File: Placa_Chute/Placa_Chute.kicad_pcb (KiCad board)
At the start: 2 copper layers, 87.5 x 55.5 mm, 34 parts, among them J1 Screw_Terminal_01x02, J2 Conn_01x02_Socket, J3 Conn_01x02, K1 JQC-3FF-012-1Z, Q1 IRF630, Q2 BC337, Q3 BC547, Q4 BC337, Q5 BC337, Q6 BC327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

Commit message: Apagar o esquemático de Ativação de Chute
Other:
- board outline removed
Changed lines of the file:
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@@
 		)
-	)
-	(gr_rect
-		(start 104.93 70.89)
-		(end 192.48 126.38)
-		(stroke
-			(width 0.05)
-			(type default)
-		)
-		(fill no)
-		(layer "Edge.Cuts")
 	)
 	(embedded_fonts no)

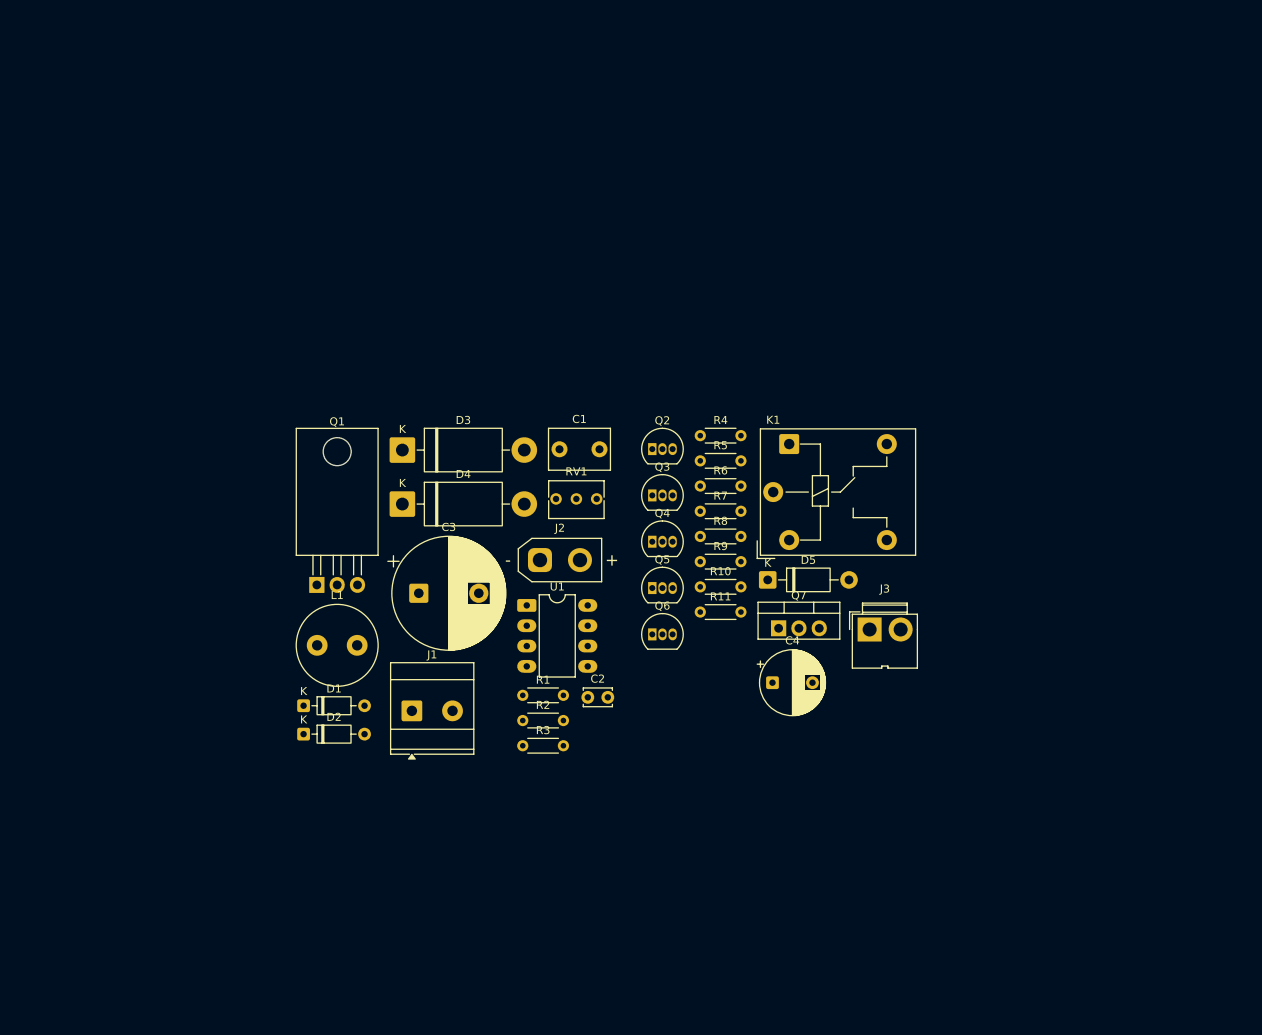
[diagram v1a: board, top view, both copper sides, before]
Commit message: Finalizando o esquemático e rearranjando a posição dos componentes na PCB
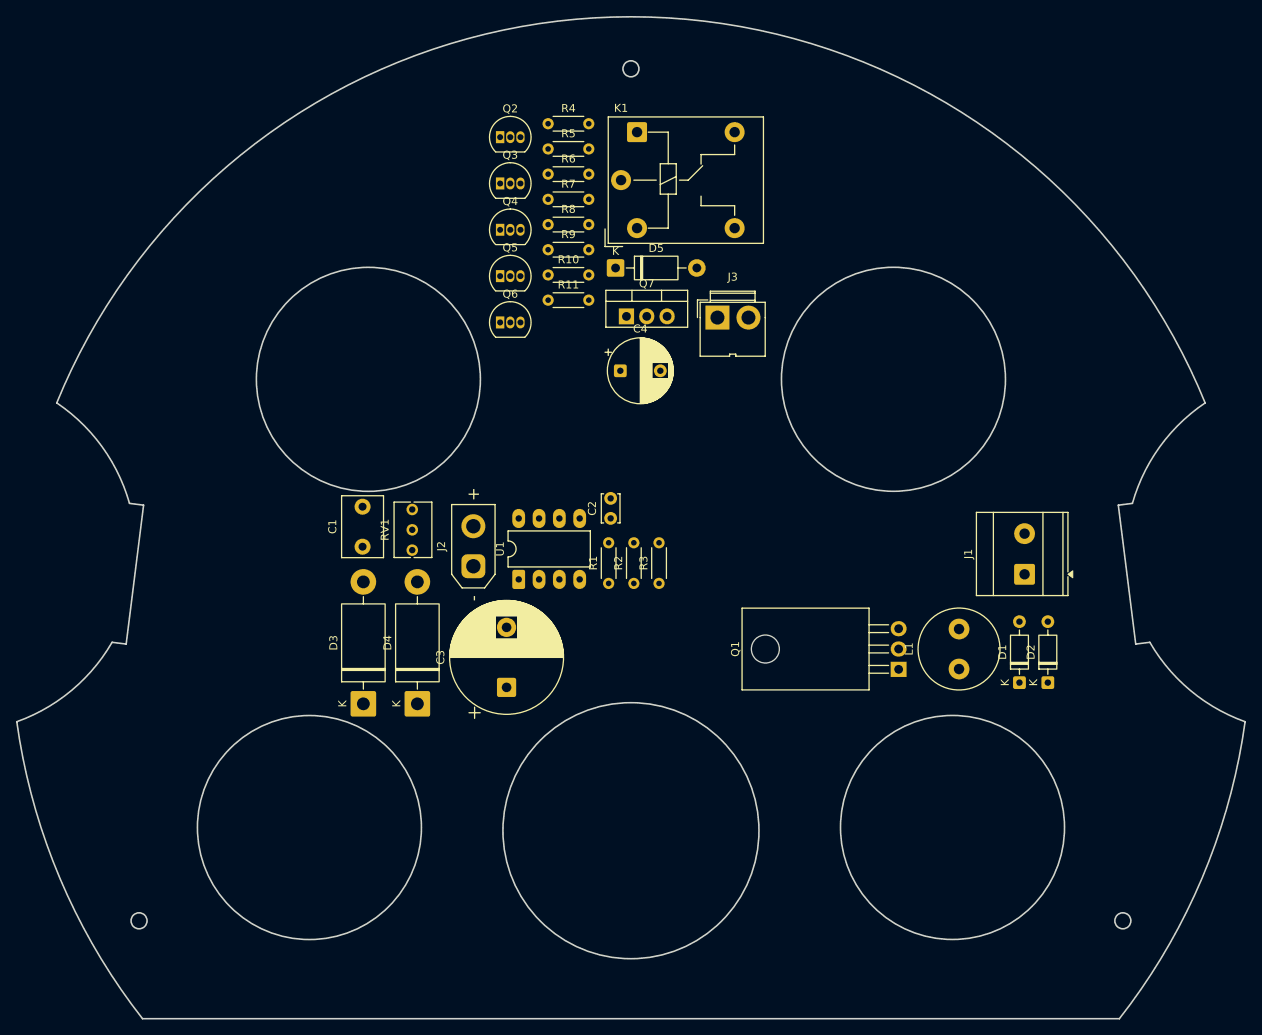
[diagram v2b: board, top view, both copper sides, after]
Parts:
- moved D2 93.3 mm to (204.9, 110.1), turned to 90 degrees
- moved D1 89.5 mm to (201.3, 110.1), turned to 90 degrees
- moved L1 80.3 mm to (193.8, 108.4), turned to 90 degrees
- moved J1 78.5 mm to (201.9, 96.6), turned to 90 degrees
- moved Q1 73.5 mm to (186.2, 108.5), turned to 90 degrees
- moved J3 43.4 mm to (163.6, 64.5)
- moved C4 43.4 mm to (151.4, 71.2)
- moved Q2 43.4 mm to (136.4, 42.0)
- moved Q4 43.4 mm to (136.4, 53.5)
- moved Q6 43.4 mm to (136.4, 65.1)
- moved Q7 43.4 mm to (152.2, 64.4)
- moved R10 43.4 mm to (142.4, 59.2)
- moved R5 43.4 mm to (142.4, 43.4)
- moved R7 43.4 mm to (142.4, 49.7)
- moved R8 43.4 mm to (142.4, 52.9)
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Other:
- board outline added: 153.5 x 125.2 mm
